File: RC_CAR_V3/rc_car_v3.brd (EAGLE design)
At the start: 160 x 100 mm, 45 parts, among them IC1 LIS2DW12TR, IC3 VNH7070BASTR, IC4 BQ34110PWR, J1 282836-2, J2 282836-2, J3 282836-2, Q2 SI2333DDS-T1-GE3, Q3 2N7002-7-F, U1 MCP1703T-3302E/DB

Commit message: PCB
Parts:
- removed IC3: VNH7070BASTR, SamacSys_Parts:SOIC127P600X175-16N
- removed PSOC1: PSOC_5LP, PSoC 5LP:PSOC
- removed Q3: 2N7002-7-F, SamacSys_Parts:SOT96P240X120-3N
- added C16: 68000-404HLF, SamacSys_Parts:HDRV4W90P0X254_1X4_1016X241X85
- added C17, C18, C19, C20, C21, C22, C23, C24: 0.1uF, SamacSys_Parts:CAPC1608X95N
- added IC2: INA199B3DCKR, SamacSys_Parts:SOT65P210X110-6N
- added J4: 282836-2, 282836-2:CONN_282836-2
- added Q1: 2N7002-7-F, SamacSys_Parts:SOT96P240X120-3N
- added Q5: SQJ912AEP-T2_BE3, SamacSys_Parts:SQJ968EPT1_GE3
- added Q7: SI7923DN-T1-E3, SamacSys_Parts:POWERPAK-1212-8_DUAL
- C3: value C0603C104K5RAC3121 -> 10uF
- IC4: value BQ34110PWR -> CY8C5888LTI-LP097; device SamacSys_Parts:SOP65P640X120-14N -> SamacSys_Parts:QFN40P800X800X100-69N
- J3: value 282836-2 -> 1-1734742-8; device 282836-2:CONN_282836-2 -> SamacSys_Parts:117347428
- Q2: value SI2333DDS-T1-GE3 -> 2N7002-7-F; device SI2333DDS-T1-GE3:SOT23 -> SamacSys_Parts:SOT96P240X120-3N
- R10: value ERA-3AED304V -> ERJ-D2DFR022V; device SamacSys_Parts:ERA3AEB101V -> SamacSys_Parts:RESC3216X80N
- R2, R4: value ERJ-UP3F1000V -> 1k
- R7: value ERJ-3RBD4302V -> 1k
- R8, R9: value ERA-3AED304V -> 1k; device SamacSys_Parts:ERA3AEB101V -> SamacSys_Parts:RESC1608X55N
- moved R3 171.5 mm to (68.3, 76.5), turned to 270 degrees
- moved R5 169.4 mm to (64.8, 76.5), turned to 270 degrees
- moved C12 161.0 mm to (82.5, 50.3), turned to 270 degrees
- moved C11 154.6 mm to (88.1, 37.8), turned to 270 degrees
- moved C9 149.0 mm to (57.7, 30.5), turned to 90 degrees
- moved C10 134.2 mm to (82.5, 37.8), turned to 270 degrees
- moved R10 130.0 mm to (75.7, 72.9), turned to 180 degrees
- moved R16 127.3 mm to (63.0, 76.5), turned to 270 degrees
- moved R12 125.9 mm to (38.9, 65.3), turned to 270 degrees
- moved R15 125.8 mm to (66.5, 76.5), turned to 270 degrees
- moved C5 122.7 mm to (72.6, 47.5)
- moved C8 119.3 mm to (88.1, 50.3), turned to 270 degrees
- moved C6 117.2 mm to (71.4, 45.2), turned to 270 degrees
- moved R9 114.4 mm to (73.9, 69.6), turned to 90 degrees
- moved C4 113.1 mm to (72.9, 45.2), turned to 270 degrees
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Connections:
- removed net BAT: IC4.4, R7.2, R8.1
- removed net DIST_1: PSOC1.P$30
- removed net DIST_2: PSOC1.P$29
- removed net DIST_3: PSOC1.P$27
- removed net GNDB_1: IC3.8
- removed net MOTOR_CURRENT: IC3.13, R16.1
- removed net N$11: IC3.6, R15.1
- removed net N$5: C3.1, IC4.7
- removed net N$6: Q2.3, R8.2
- removed net N$8: Q2.1, Q3.3, R10.1
- removed net OUTA: IC3.2, J3.1
- removed net OUTB: IC3.7, J3.2
- removed net PWM: IC3.11, R14.2
- removed net PWM1: PSOC1.P$5, R16.2
- removed net SRP: J1.2, R1.1, R4.2
- removed net VEN: IC4.1, Q3.1
- new net D1: J4.1, Q5.5, Q5.7, Q5.9, Q7.7, Q7.8
- new net D2: J4.2, Q5.10, Q5.6, Q5.8, Q7.5, Q7.6
- new net FWD: Q1.3, Q7.4, R14.1
- new net IMOTOR: C24.1, IC4.51, R9.1
- new net ISENSE: IC2.6, IC4.31
- new net N$16: C21.2, IC4.16
- new net N$21: J3.6, J3.8
- new net RVRS: Q2.3, Q7.2, R13.1
- new net SRC: Q5.1, Q5.3, R10.2, R9.2
- new net SWDCK: IC4.12, J3.2
- new net SWDIO: IC4.11, J3.3
- new net VBAT: C3.1, IC4.34, R2.2, R7.1
- new net XRES: IC4.10, J3.4
- net 0: now also C16.3, C16.4, C17.1, C18.2, C19.1, C20.1, C21.1, C22.2, C23.2, C24.2, IC2.1, IC2.2, IC4.25, IC4.5, IC4.69, IC4.7, IC4.9, J1.2, J2.2, Q1.2, Q2.2, R10.1, R2.1; no longer IC3.1, IC3.16, IC3.9, PSOC1.P$26, PSOC1.P$51, Q3.2, R1.2, R2.2, R7.1
- net 3.3V: now also IC2.3, R4.2, R8.2; no longer IC4.6, R3.2, R5.2
- net CTS: now also IC4.3; no longer PSOC1.P$38
- net CTS_JETSON: now also IC4.52; no longer PSOC1.P$34
- net ECHO_1: now also IC4.65
- net ECHO_2: now also IC4.64
- net ECHO_3: now also IC4.62
- net FORWARD: now also IC4.49, R15.2, R3.2; no longer PSOC1.P$50, R13.2
- net N$10: now also C17.2, C18.1, IC4.26, IC4.57; no longer IC3.3, R13.1
- net N$13: now also Q1.1, R16.1; no longer J2.2
- net N$2: now also Q5.2, R3.1; no longer R10.2, R9.1
- net N$3: now also IC2.4, J1.1, R1.1; no longer IC4.10, R2.1
- net N$4: now also Q2.1, R15.1; no longer IC4.9, R4.1
- net N$7: now also Q5.4, R5.1; no longer PSOC1.P$49, R14.1
- net REVERSE: now also IC4.56, R16.2, R5.2; no longer PSOC1.P$4, R15.2
- net RTS: now also IC4.4; no longer PSOC1.P$37
- net RTS_JETSON: now also IC4.54; no longer PSOC1.P$33
- net RX: now also IC4.20; no longer PSOC1.P$40
- net RX_JETSON: now also IC4.47; no longer PSOC1.P$36
- net SCL: now also IC4.38, R8.1; no longer IC4.13, PSOC1.P$42, R3.1
- net SDA: now also IC4.39, R4.1; no longer IC4.14, PSOC1.P$41, R5.1
- net SERVO: now also C16.2, IC4.68; no longer PSOC1.P$32
- net SPEED: now also IC4.60; no longer PSOC1.P$13
- net TRIG: now also IC4.66; no longer PSOC1.P$31
- net TX: now also IC4.21; no longer PSOC1.P$39
- net TX_JETSON: now also IC4.46; no longer PSOC1.P$35
- net VBUS: now also C16.1, IC2.5, Q7.1, Q7.3, R1.2, R13.2, R14.2, R7.2; no longer IC3.12, IC3.4, IC3.5, J1.1, Q2.2, R9.2
- net VDD: now also C19.2, C20.2, C22.1, C23.1, IC4.17, IC4.24, IC4.35, IC4.59, IC4.67; no longer PSOC1.P$1, PSOC1.P$52
- net VSENSE: now also IC4.33
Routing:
- net 3.3V: track 0.00 -> 134.8 mm, vias 0 -> 5
- net VDD: track 0.00 -> 105.8 mm, vias 0 -> 8
- net 5V: track 0.00 -> 103.7 mm, vias 0 -> 1
- net RTS: track 0.00 -> 59.8 mm, vias 0 -> 4
- net ECHO_1: track 0.00 -> 59.2 mm, vias 0 -> 5
- net CTS: track 0.00 -> 58.4 mm, vias 0 -> 4
- net ECHO_2: track 0.00 -> 57.4 mm, vias 0 -> 3
- net ISENSE: track 0.00 -> 50.2 mm, vias 0 -> 4
- net CTS_JETSON: track 0.00 -> 45.2 mm, vias 0 -> 2
- net RX: track 0.00 -> 43.9 mm, vias 0 -> 4
- net RTS_JETSON: track 0.00 -> 43.8 mm, vias 0 -> 3
- net RX_JETSON: track 0.00 -> 43.4 mm, vias 0 -> 1
- net TX_JETSON: track 0.00 -> 43.3 mm, vias 0 -> 1
- net TX: track 0.00 -> 42.0 mm, vias 0 -> 2
- net ECHO_3: track 0.00 -> 40.3 mm, vias 0 -> 5
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- added copper zone on layer 1, net 5V
- added copper zone on layer 1, net D1
- added copper zone on layer 16, net D1
- added copper zone on layer 1, net D2
- added copper zone on layer 1, net N$3
- added copper zone on layer 1, net SRC
- removed copper zone on layer 1, net SRP
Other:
- board size 160 x 100 mm -> 91.7 x 68 mm

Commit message: Added more connections
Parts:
- added C25, C26: 0.1uF, SamacSys_Parts:CAPC1608X95N
- moved C3 19.8 mm to (47.0, 62.0)
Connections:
- new net N$6: C25.2, IC4.42
- net 0: now also C25.1, C26.1, IC4.43, IC4.45
- net VDD: now also C26.2, IC4.44
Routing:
- net 5V: track 103.7 -> 134.1 mm
- net VBUS: track 7.80 -> 19.0 mm
- net VBAT: track 32.4 -> 28.6 mm

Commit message: PCB changes
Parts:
- moved R4 0.57 mm to (53.3, 58.2)
- moved C26 0.51 mm to (55.9, 51.8)
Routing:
- net 3.3V: track 134.8 -> 126.9 mm
- net TX_JETSON: track 43.3 -> 35.7 mm
- net VDD: track 105.8 -> 99.5 mm
- net SDA: track 30.9 -> 24.7 mm, vias 2 -> 1
- net RX_JETSON: track 43.4 -> 37.3 mm
- net SCL: track 30.6 -> 27.3 mm, vias 2 -> 1

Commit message: Changes
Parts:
- moved C25 70.4 mm to (71.1, 37.3)
- moved C26 6.91 mm to (53.8, 58.4)
- moved R4 1.27 mm to (52.1, 58.2)
- moved C22 1.02 mm to (48.3, 58.4)
- moved R8 1.02 mm to (50.0, 58.4)

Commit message: Changes
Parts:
- moved U1 33.3 mm to (34.8, 53.7)
- moved C25 27.0 mm to (54.4, 58.5), turned to 90 degrees
- moved J2 19.7 mm to (18.8, 32.1), turned to 180 degrees
- moved D2 16.1 mm to (33.4, 42.5)
- moved R17 16.1 mm to (38.0, 42.5)
- moved C7 15.0 mm to (35.3, 35.1)
- moved C2 13.4 mm to (73.0, 32.1)
- moved XB1 13.4 mm to (54.0, 40.0)
- moved C9 13.4 mm to (71.0, 32.1)
- moved R6 13.3 mm to (33.7, 47.5)
- moved C1 11.6 mm to (24.3, 78.9)
- moved IC2 11.6 mm to (21.0, 78.4)
- moved J1 11.6 mm to (16.4, 89.3)
- moved R1 11.6 mm to (16.4, 78.6)
- moved C15 10.8 mm to (28.3, 88.8)
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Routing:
- net 3.3V: track 126.9 -> 82.9 mm
- net 5V: track 134.4 -> 109.0 mm
- net VDD: track 99.5 -> 82.9 mm
- net TX: track 42.0 -> 55.6 mm
- net RX: track 43.9 -> 55.7 mm, vias 4 -> 2
- net VBUS: track 19.0 -> 7.80 mm
- net CTS: track 58.4 -> 49.6 mm
- net ISENSE: track 50.2 -> 42.2 mm
- net RTS: track 59.8 -> 54.1 mm
- net VBAT: track 28.6 -> 23.4 mm
- net N$6: track 0.00 -> 4.00 mm
- net SDA: track 24.7 -> 28.3 mm
- net SCL: track 27.3 -> 30.4 mm
- net N$9: track 2.63 -> 0.00 mm
- net IMOTOR: track 30.9 -> 29.7 mm
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- removed copper zone on layer 1, net 0
- removed copper zone on layer 1, net 5V
- removed copper zone on layer 1, net N$3
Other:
- board size 91.7 x 68 mm -> 79.5 x 68 mm

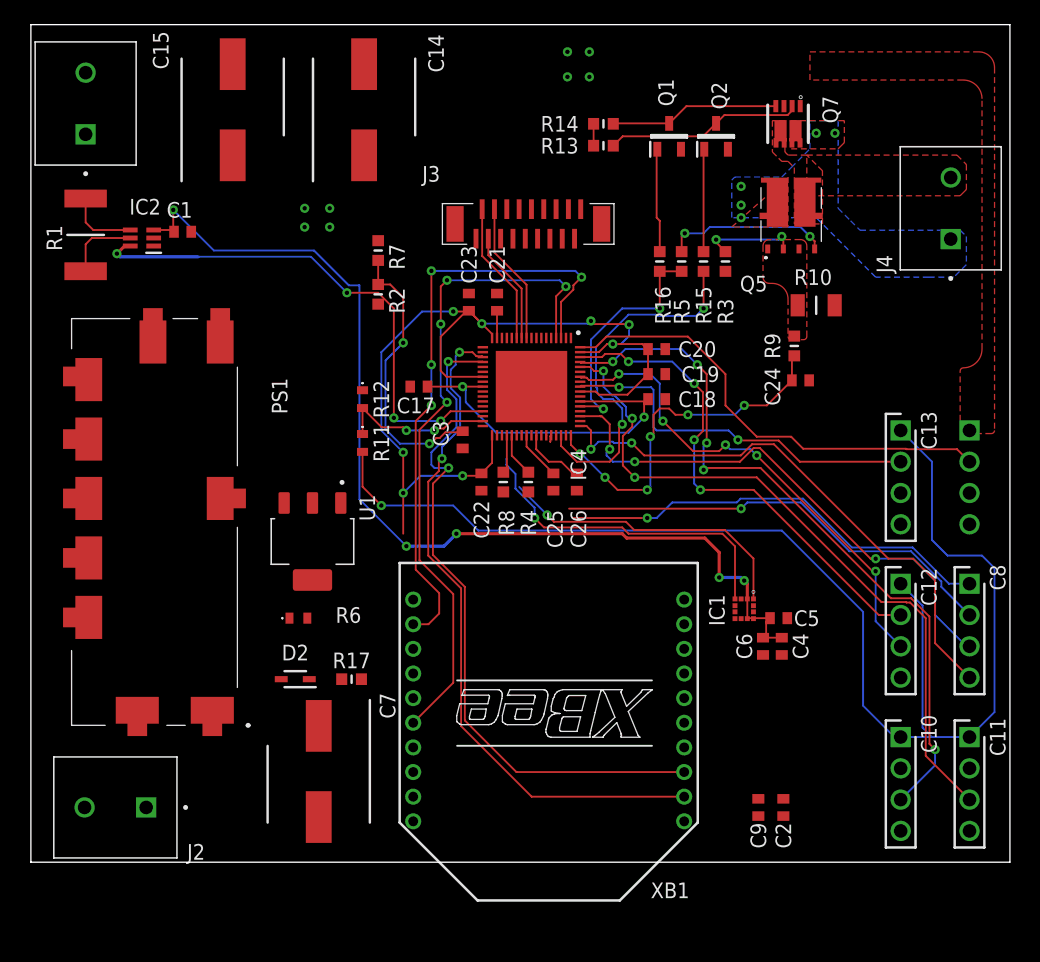
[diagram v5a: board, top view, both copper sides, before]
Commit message: Added ground planes
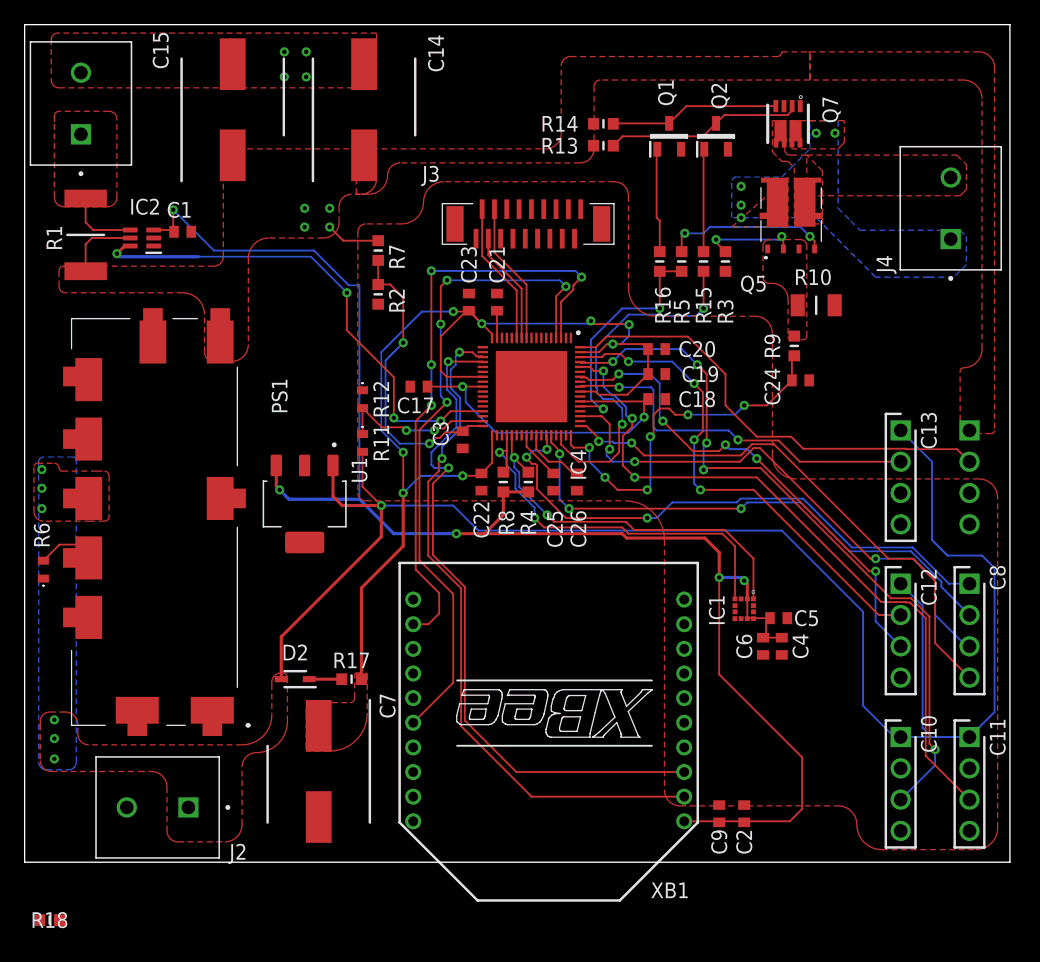
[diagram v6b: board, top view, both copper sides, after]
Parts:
- added R18: 1k, SamacSys_Parts:RESC1608X55N
- moved R6 21.1 mm to (13.0, 51.4), turned to 90 degrees
- moved J2 3.43 mm to (22.2, 32.1)
- moved C2 3.22 mm to (69.8, 31.6)
- moved C9 3.22 mm to (67.8, 31.6)
- moved U1 3.11 mm to (34.2, 56.8)
- moved J1 0.38 mm to (16.0, 89.3)
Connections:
- new net N$5: IC4.37, R18.2
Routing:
- net 3.3V: track 82.9 -> 128.7 mm
- net 5V: track 109.0 -> 133.2 mm, vias 1 -> 7
- net VDD: track 82.9 -> 96.1 mm
- net TX_JETSON: track 35.7 -> 45.8 mm, vias 1 -> 3
- net RX_JETSON: track 37.3 -> 43.3 mm, vias 1 -> 3
- net N$1: track 0.00 -> 5.08 mm
- net SDA: track 28.3 -> 30.9 mm, vias 1 -> 2
- net N$9: track 0.00 -> 2.63 mm
- net VBUS: track 7.80 -> 10.4 mm
- net VBAT: track 23.4 -> 25.3 mm
- net ISENSE: track 42.2 -> 40.7 mm
- net SCL: track 30.4 -> 31.8 mm, vias 1 -> 2
- net CTS_JETSON: track 45.2 -> 43.9 mm
- net IMOTOR: track 29.7 -> 30.4 mm
- added copper zone on layer 1, net 0
- added copper zone on layer 1, net 5V
- added copper zone on layer 16, net 5V
- added copper zone on layer 1, net N$3
- added copper zone on layer 1, net VDD
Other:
- board size 79.5 x 68 mm -> 80 x 68 mm

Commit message: Changes
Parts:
- moved R18 51.1 mm to (36.4, 68.6)
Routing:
- added copper zone on layer 16, net 0

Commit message: Done
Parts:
- added LED1: LTST-C191TBKT, SamacSys_Parts:LEDC1608X65N
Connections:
- removed net N$5: IC4.37, R18.2
- new net LED: IC4.29, R18.2
- new net N$8: LED1.1, R18.1
- net 5V: now also LED1.2
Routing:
- net LED: track 0.00 -> 16.1 mm, vias 0 -> 2
- net 5V: track 133.2 -> 139.1 mm
- net N$8: track 0.00 -> 4.35 mm
